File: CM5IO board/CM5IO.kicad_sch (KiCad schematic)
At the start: 8 parts

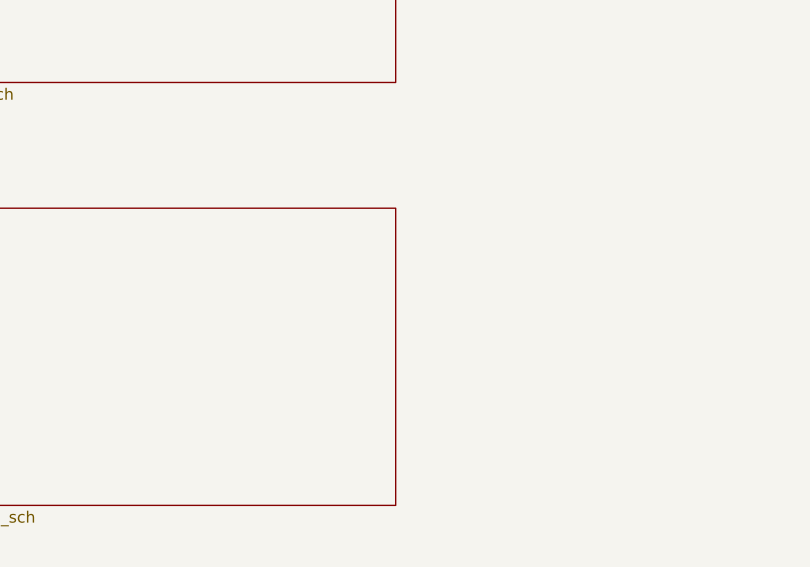
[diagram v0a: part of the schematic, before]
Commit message: Continued boost design
R4, C1, C2, C3 selected
R4, L1 unsure
COMP, EN yet to be finished.
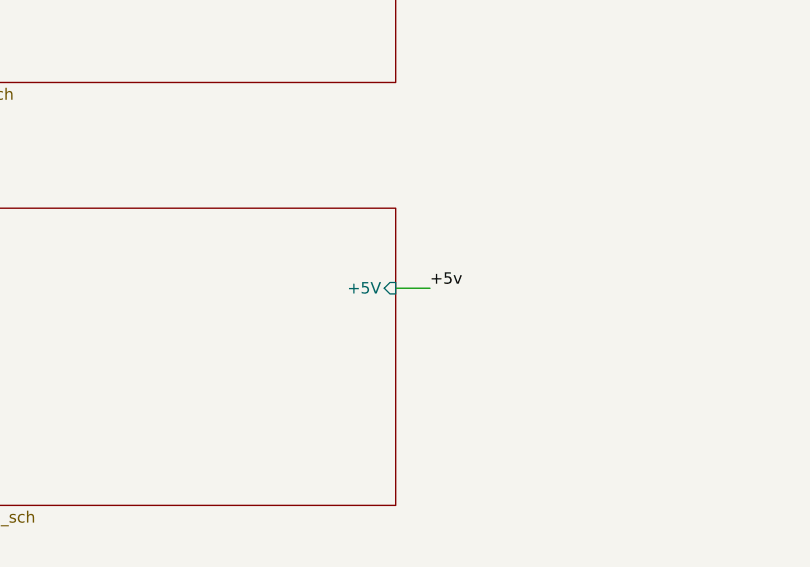
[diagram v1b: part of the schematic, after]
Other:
- sheet Buck Boost ports: added +5V; removed none
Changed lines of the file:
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@@
+	(wire
+		(pts
+			(xy 88.9 125.73) (xy 92.71 125.73)
+		)
+		(stroke
+			(width 0)
+			(type default)
+		)
+	)
 	(wire
 		(pts
@@
 	(label "+3.3v"
 		(at 234.95 118.11 0)
+		(effects
+			(font
+				(size 1.27 1.27)
+			)
+			(justify left bottom)
+		)
+	)
+	(label "+5v"
+		(at 92.71 125.73 0)
 		(effects
 			(font
@@
 			)
 		)
+		(pin "+5V" input
+			(at 88.9 125.73 0)
+			(effects
+				(font
+					(size 1.27 1.27)
+				)
+				(justify right)
+			)
+		)
